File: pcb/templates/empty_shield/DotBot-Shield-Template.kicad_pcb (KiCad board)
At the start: 4 copper layers, 29 x 27 mm, 3 parts, among them J1 Bottom Header, J2 Left Header, J3 Right Header

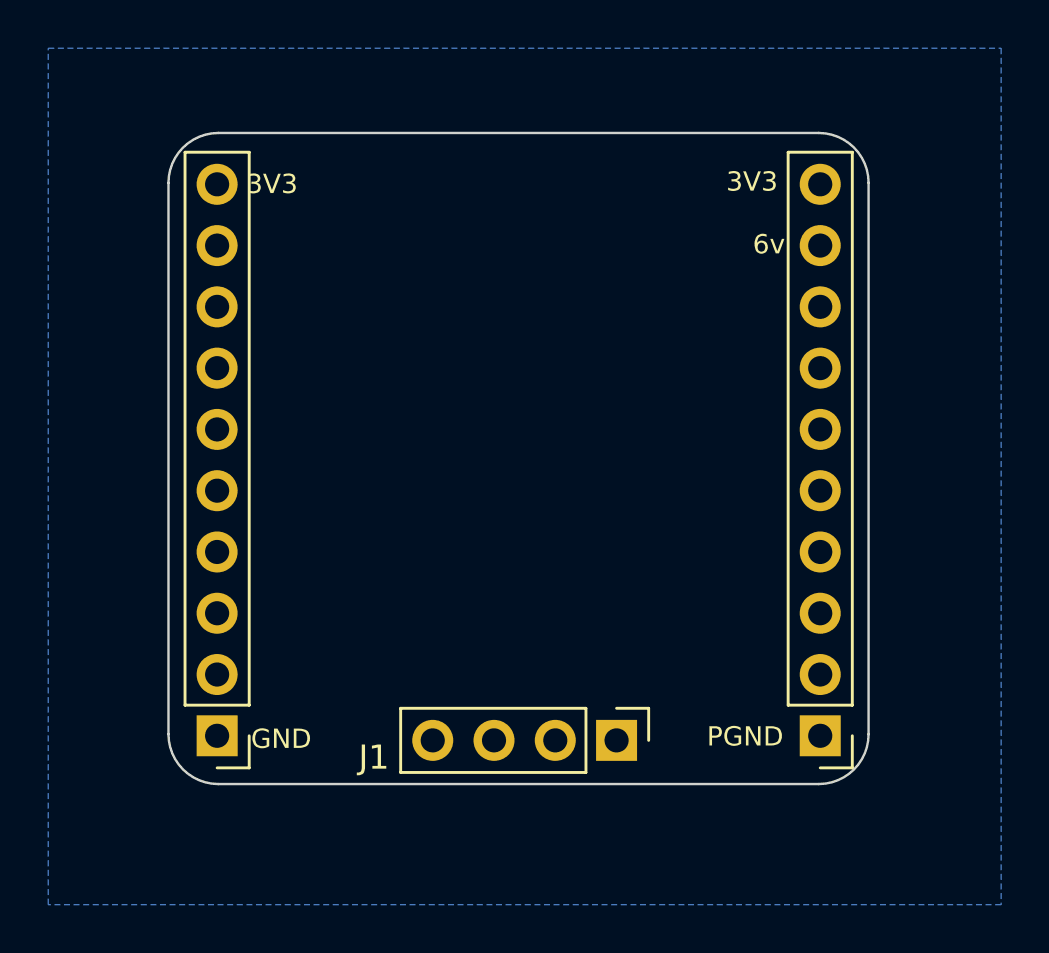
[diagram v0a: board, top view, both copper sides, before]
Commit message: #12 Flip header on the template shield.
So that the 3D render looks correct with the Left and Right headers pointing to the bottom
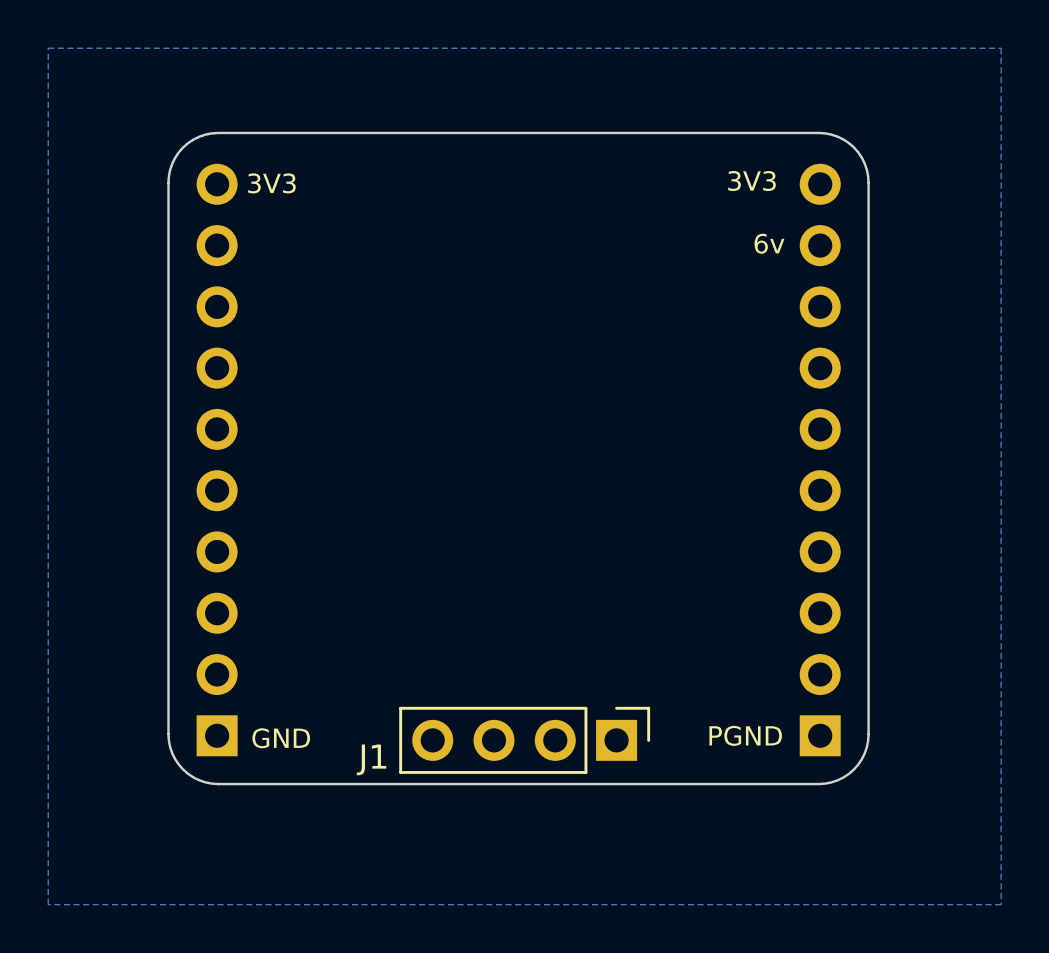
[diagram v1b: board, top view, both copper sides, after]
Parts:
- J2, J3: moved to B.Cu
- turned J2 to 0 degrees
- turned J3 to 0 degrees
